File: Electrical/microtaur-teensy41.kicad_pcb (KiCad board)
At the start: 2 copper layers, 150.7 x 116 mm, 33 parts, among them J1 Conn_01x06, J2 USB_A, U1 Teensy4.1, U3 LM7805_TO220

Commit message: Add files via upload
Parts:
- removed J1: Conn_01x06, Connector_JST:JST_SH_SM06B-SRSS-TB_1x06-1MP_P1.00mm_Horizontal
- U3: footprint Package_TO_SOT_THT:TO-220-3_Horizontal_TabDown -> Package_TO_SOT_SMD:SOT-223
- moved J2 74.0 mm to (128.1, 121.3), turned to 90 degrees
- moved IMU1 24.5 mm to (157.3, 116.3), turned to 180 degrees
- moved R1 23.9 mm to (137.7, 123.1), turned to 90 degrees
- moved R2 20.0 mm to (142.3, 123.1), turned to 270 degrees
- moved U3 10.7 mm to (147.1, 126.5)
- moved C1 8.02 mm to (140.5, 133.8), turned to 180 degrees
- moved U1 5.85 mm to (140.3, 89.8)
- moved PWR1 5.78 mm to (139.7, 165.5), turned to 90 degrees
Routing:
- net /5V: track 238.6 -> 149.3 mm, vias 1 -> 0
- net /RX8: track 122.0 -> 36.0 mm
- net /RX7: track 124.2 -> 47.4 mm
- net GND: track 729.4 -> 801.8 mm, vias 2 -> 0
- net /TX8: track 111.9 -> 40.6 mm
- net /TX7: track 117.2 -> 54.4 mm
- net Vdrive: track 246.1 -> 283.5 mm
- net /PS2_CMD: track 33.6 -> 0.00 mm
- net /PS2_DAT: track 32.6 -> 0.00 mm
- net /D+: track 84.8 -> 54.6 mm
- net /SCL: track 15.2 -> 42.9 mm
- net /SDA: track 13.4 -> 40.6 mm
- net /D-: track 85.9 -> 61.0 mm
- net /PS2_CLK: track 24.9 -> 0.00 mm
- net /RX2: track 74.5 -> 99.1 mm, vias 2 -> 0
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- removed copper zone on B.Cu, net (none)

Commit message: added package3d in pcb
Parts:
- ?: renamed from MPOW6; value Conn_01x02 -> (none)
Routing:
- net Vdrive: track 283.5 -> 285.0 mm
- net GND: track 801.8 -> 802.6 mm
- added copper zone on F.Cu, net GND
- added copper zone on B.Cu, net Vdrive

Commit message: Add files via upload
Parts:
- MPOW6: renamed from ?; value (none) -> Conn_01x02
- moved MPOW6 2.62 mm to (110.5, 108.4)
- moved MPOW3 2.62 mm to (84.5, 108.4)
- moved MPOW1 1.15 mm to (84.4, 125.1)
- moved MPOW2 0.90 mm to (110.4, 124.9)
- moved SER7 0.20 mm to (111.3, 146.0)
- moved SER8 0.20 mm to (168.7, 146.0)
- moved SER1 0.20 mm to (111.3, 86.0)
- moved SER5 0.20 mm to (168.7, 86.0)
- moved SER2 0.15 mm to (70.2, 86.0)
- moved SER3 0.15 mm to (209.8, 146.0)
- moved SER4 0.15 mm to (209.8, 86.0)
- moved SER6 0.15 mm to (70.2, 146.0)
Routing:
- net GND: track 802.6 -> 516.0 mm
- net Vdrive: track 285.0 -> 54.4 mm
- net /TX3: track 86.3 -> 92.9 mm
- net /RX3: track 89.4 -> 95.5 mm
- net /TX4: track 82.9 -> 80.1 mm
- net /RX6: track 94.6 -> 97.3 mm
- net /RX4: track 84.5 -> 82.5 mm
- net /TX6: track 97.8 -> 99.7 mm
- net /RX1: track 55.3 -> 56.5 mm
- added copper zone on B.Cu, net GND
- added copper zone on F.Cu, net Vdrive
- removed copper zone on F.Cu, net GND
- removed copper zone on B.Cu, net Vdrive
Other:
- rule trace_min: 0.2 -> 0

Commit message: Add files via upload
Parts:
- moved J2 28.5 mm to (134.7, 149.0)
- moved MPOW4 12.4 mm to (199.4, 125.1)
- moved MPOW7 12.4 mm to (199.4, 108.4)
- moved MPOW3 8.76 mm to (75.7, 108.4)
- moved MPOW1 8.64 mm to (75.7, 125.4)
- moved MPOW6 5.33 mm to (105.2, 108.4)
- moved MPOW2 5.17 mm to (105.2, 125.1)
- moved MPOW5 2.54 mm to (170.5, 124.9)
- moved MPOW8 2.54 mm to (170.5, 108.4)
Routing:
- net GND: track 516.0 -> 434.2 mm
- net /D+: track 54.6 -> 77.1 mm
- net /D-: track 61.0 -> 81.0 mm
- net Vdrive: track 54.4 -> 37.2 mm
- net /5V: track 149.3 -> 163.7 mm
- net /RX1: track 56.5 -> 46.3 mm
- net /TX6: track 99.7 -> 105.9 mm
- net /RX6: track 97.3 -> 102.0 mm
- net /RX2: track 99.0 -> 95.1 mm
- net /TX2: track 84.7 -> 86.6 mm
- net /SCL: track 42.9 -> 44.1 mm
- net /TX3: track 92.9 -> 94.1 mm
- net /RX3: track 95.5 -> 96.6 mm
- net /RX4: track 82.5 -> 83.1 mm

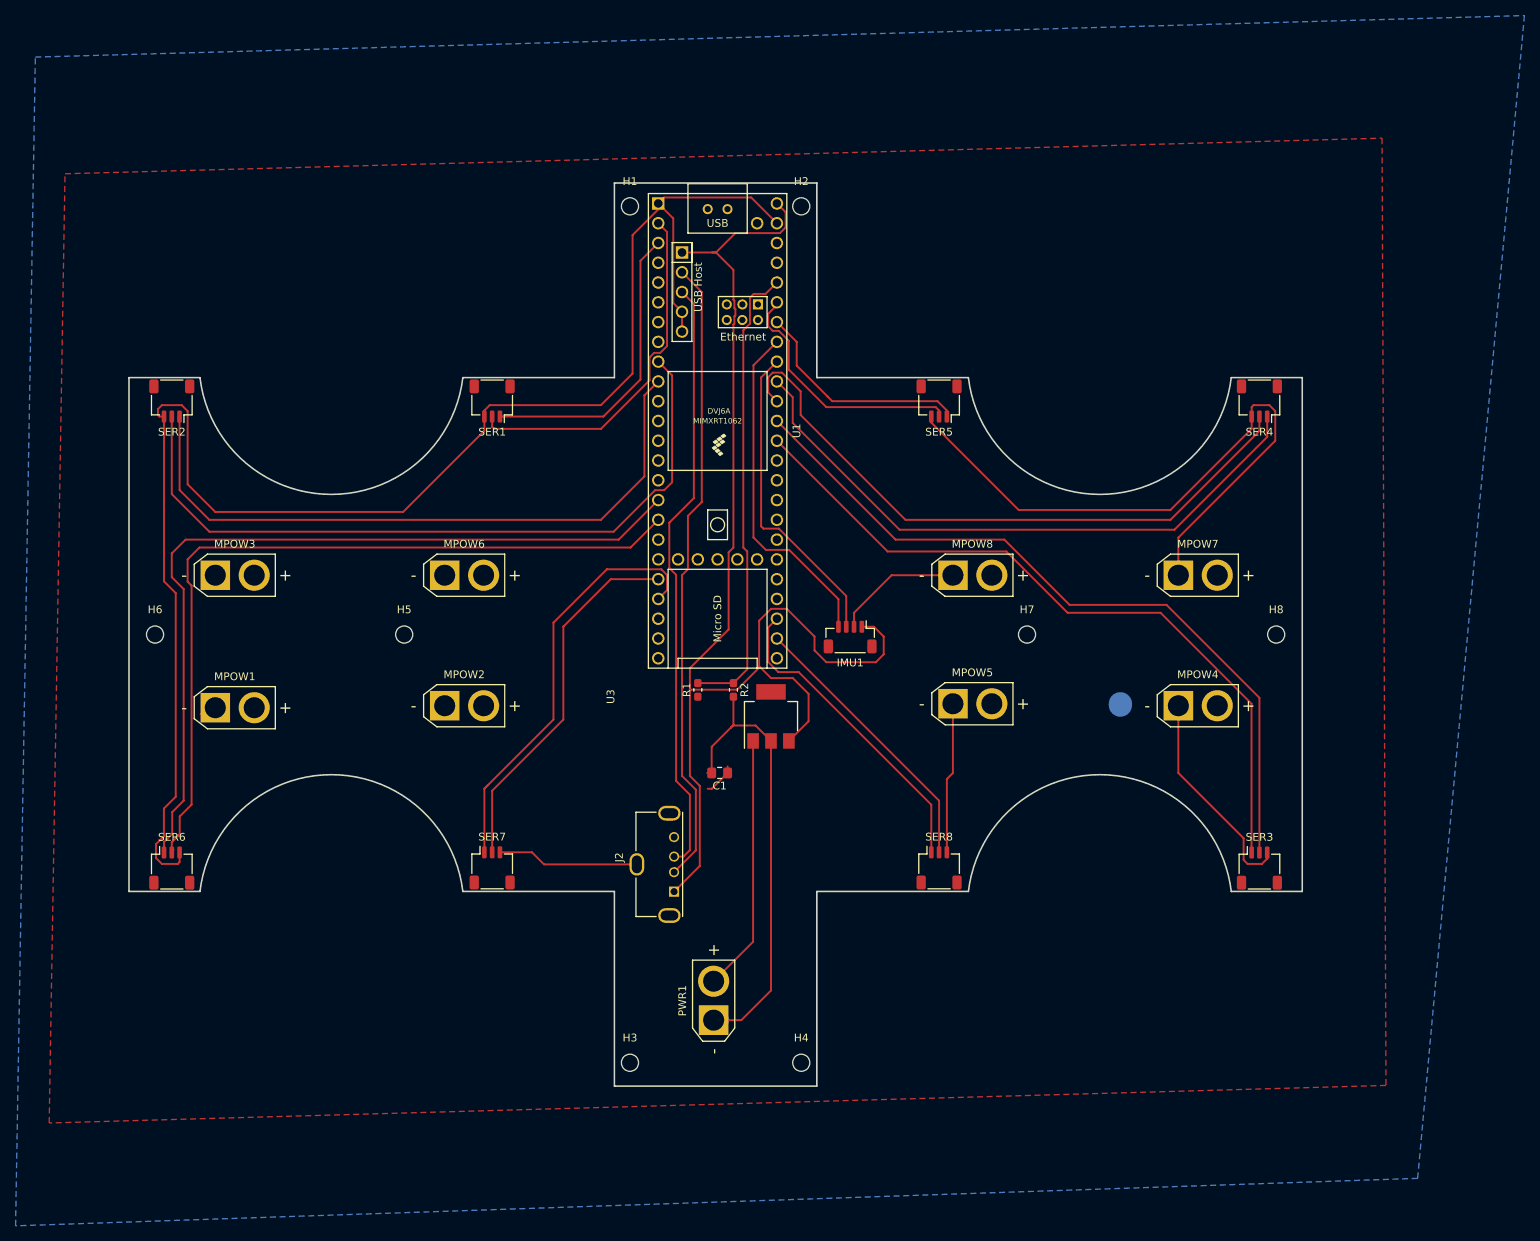
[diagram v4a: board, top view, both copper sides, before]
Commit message: Updated pcb to check compatibility with mcad
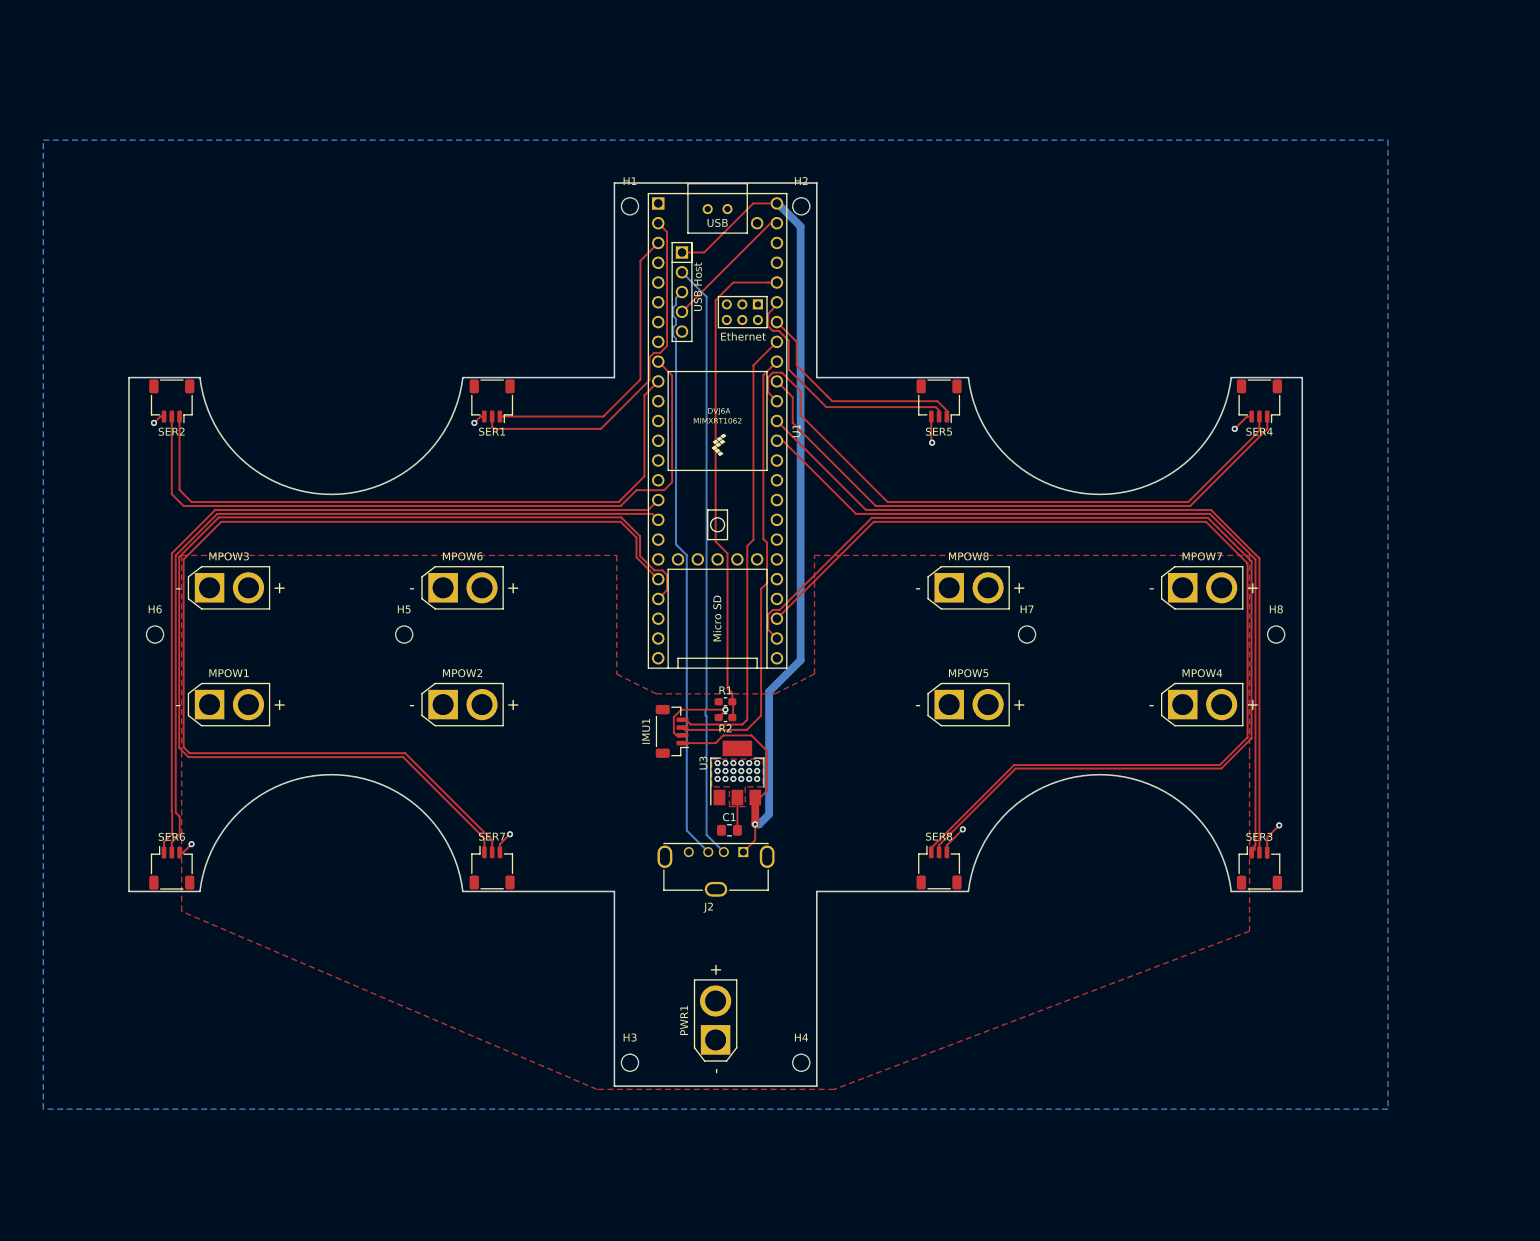
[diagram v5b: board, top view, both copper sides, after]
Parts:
- moved IMU1 25.9 mm to (134.4, 128.4), turned to 90 degrees
- moved J2 10.2 mm to (143.6, 143.9), turned to 180 degrees
- moved U3 8.45 mm to (142.8, 133.8)
- moved C1 7.47 mm to (141.8, 141.1), turned to 0 degrees
- moved R1 3.87 mm to (141.3, 124.6), turned to 0 degrees
- moved R2 3.70 mm to (141.3, 126.7), turned to 180 degrees
- moved PWR1 2.55 mm to (140.0, 168.1)
- moved MPOW3 1.78 mm to (75.0, 110.0)
- moved MPOW7 1.72 mm to (200.0, 110.0)
- moved MPOW8 1.69 mm to (170.0, 110.0)
- moved MPOW6 1.63 mm to (105.0, 110.0)
- moved MPOW1 0.84 mm to (75.0, 125.0)
- moved MPOW4 0.58 mm to (200.0, 125.0)
- moved MPOW5 0.49 mm to (170.0, 125.0)
- moved MPOW2 0.25 mm to (105.0, 125.0)
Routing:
- net GND: track 434.2 -> 58.6 mm, vias 0 -> 27
- net /RX8: track 36.1 -> 142.6 mm
- net /TX8: track 40.7 -> 137.2 mm
- net /RX7: track 47.5 -> 137.8 mm
- net /TX7: track 54.9 -> 143.2 mm
- net /5V: track 163.7 -> 125.3 mm, vias 0 -> 1
- net Vdrive: track 37.2 -> 0.00 mm
- net /SDA: track 40.6 -> 57.7 mm
- net /SCL: track 44.1 -> 58.9 mm
- net /TX3: track 94.1 -> 105.6 mm
- net /RX3: track 96.6 -> 107.1 mm
- net /D-: track 81.0 -> 76.8 mm
- net /BAT_MON: track 59.6 -> 63.4 mm
- net /TX4: track 80.4 -> 77.2 mm
- net /RX2: track 95.1 -> 92.4 mm
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- added copper zone on F.Cu, net GND

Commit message: completed pcb design, ready to fab
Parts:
- removed H1, H2: MountingHole, MountingHole:MountingHole_2.2mm_M2
- IMU1: footprint Connector_JST:JST_SH_BM04B-SRSS-TB_1x04-1MP_P1.00mm_Vertical -> Connector_JST:JST_SH_SM04B-SRSS-TB_1x04-1MP_P1.00mm_Horizontal
- moved IMU1 12.5 mm to (146.3, 124.9)
- moved J2 7.01 mm to (138.7, 149.0), turned to 270 degrees
- moved PWR1 1.27 mm to (140.0, 169.3)
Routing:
- net /SCL: track 58.9 -> 46.7 mm
- net /D+: track 74.6 -> 86.6 mm
- net /SDA: track 57.7 -> 45.8 mm
- net /D-: track 76.8 -> 85.0 mm
- net /5V: track 125.3 -> 126.2 mm
- net GND: vias 27 -> 26
